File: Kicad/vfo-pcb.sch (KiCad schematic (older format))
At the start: 56 parts, among them J10 Link-out 1a, J11 RxTx, J13 Link-out 1b, J14 V12, J17 Link-out 2a, J18 Link-out 3, J19 Link-out 2b, J2 Conn_01x07_Female, J3 Si5351, J4 ESP32L, J5 ESP32R, J6 Rotery Encoder1, J7 ILI9341, J8 Rotery Encoder2, J9 Analog in 3-6, SW1 Rotary_Encoder_Switch, U1 AS179-92LF, U2 74HC595, U3 L7805, U4 AS179-92LF

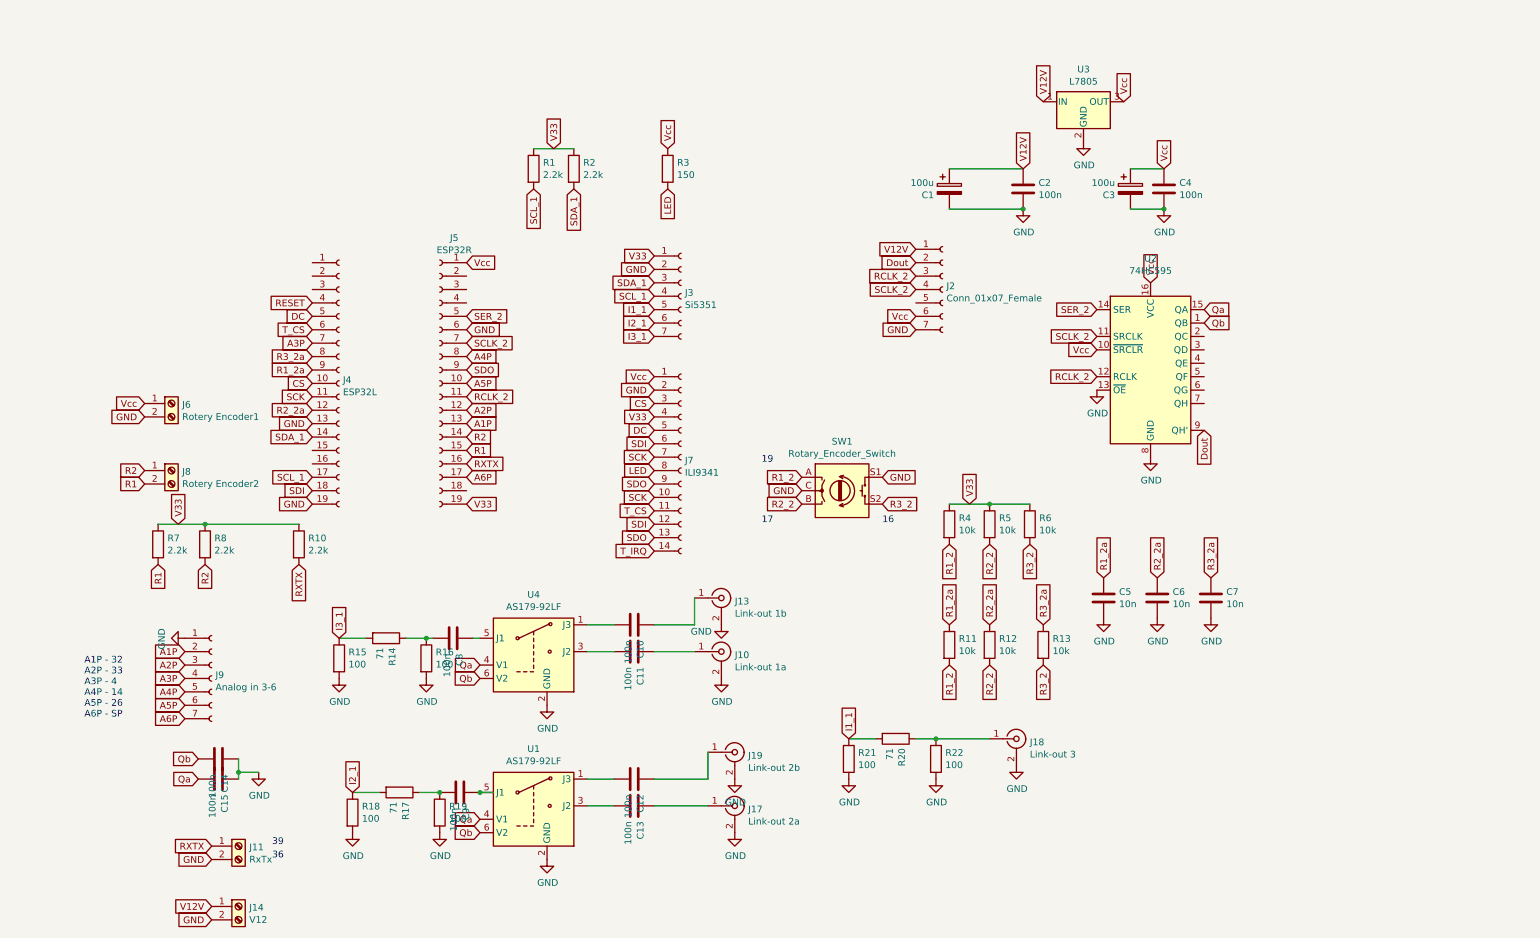
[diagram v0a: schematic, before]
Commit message: Attenuator removed
To improve crosstalk the attenuators are removed and replaced by 100nF DC blocker
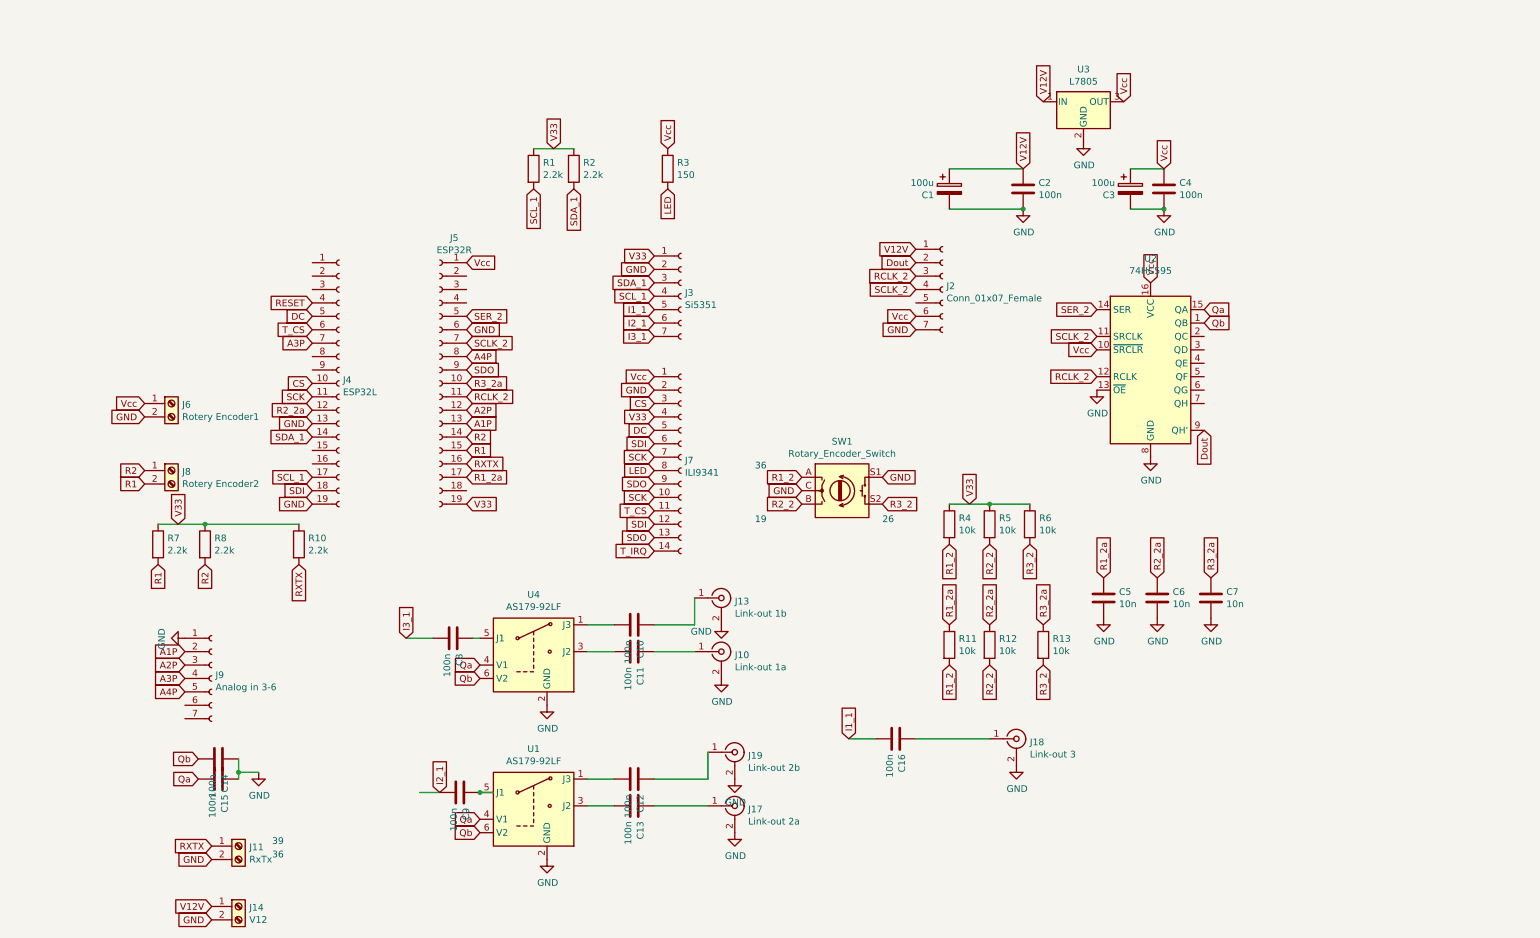
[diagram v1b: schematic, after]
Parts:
- removed R14, R17, R20: 71, Resistor_SMD:R_1206_3216Metric_Pad1.42x1.75mm_HandSolder, symbol Device:R
- removed R15, R16, R18, R19, R21, R22: 100, Resistor_SMD:R_1206_3216Metric_Pad1.42x1.75mm_HandSolder, symbol Device:R
- added C16: 100n, Capacitor_SMD:C_1206_3216Metric_Pad1.42x1.75mm_HandSolder, symbol Device:C
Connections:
- net labels removed: A5P, A6P
- wire segments 32 -> 28
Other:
- note added: "26"
- note removed: "16"
- note removed: "17"
- note removed: "A1P - 32\nA2P - 33\nA3P - 4\nA4P - 14\nA5P - 26\nA6P - SP"
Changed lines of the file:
@@
 Text GLabel 6400 4100 0    50   Input ~ 0
 R2_2
-Text GLabel 2750 3100 0    50   Input ~ 0
+Text GLabel 3900 3900 2    50   Input ~ 0
 R1_2a
-Text GLabel 2750 3400 0    50   Input ~ 0
-R2_2a
 Text GLabel 7000 4100 2    50   Input ~ 0
 R3_2
-Text GLabel 2750 3000 0    50   Input ~ 0
+Text GLabel 3900 3200 2    50   Input ~ 0
 R3_2a
 Text GLabel 7000 3900 2    50   Input ~ 0
@@
 Text GLabel 6750 5850 1    50   Input ~ 0
 I1_1
-Text GLabel 3050 6250 1    50   Input ~ 0
+Text GLabel 3700 6250 1    50   Input ~ 0
 I2_1
 $Comp
@@
 Text GLabel 8650 4650 1    50   Input ~ 0
 R1_2a
-$Comp
-L power:GND #PWR014
-U 1 1 5DAB08FF
-P 2950 5400
-F 0 "#PWR014" H 2950 5150 50  0001 C CNN
-F 1 "GND" H 2955 5227 50  0000 C CNN
-F 2 "" H 2950 5400 50  0001 C CNN
-F 3 "" H 2950 5400 50  0001 C CNN
-	1    2950 5400
-	1    0    0    -1
-$EndComp
-$Comp
-L Device:R R15
-U 1 1 5DABA121
-P 2950 5250
-F 0 "R15" H 3020 5296 50  0000 L CNN
-F 1 "100" H 3020 5205 50  0000 L CNN
-F 2 "Resistor_SMD:R_1206_3216Metric_Pad1.42x1.75mm_HandSolder" V 2880 5250 50  0001 C CNN
-F 3 "~" H 2950 5250 50  0001 C CNN
-	1    2950 5250
-	1    0    0    -1
-$EndComp
-$Comp
-L power:GND #PWR015
-U 1 1 5DABB0D6
-P 3600 5400
-F 0 "#PWR015" H 3600 5150 50  0001 C CNN
-F 1 "GND" H 3605 5227 50  0000 C CNN
-F 2 "" H 3600 5400 50  0001 C CNN
-F 3 "" H 3600 5400 50  0001 C CNN
-	1    3600 5400
-	1    0    0    -1
-$EndComp
-$Comp
-L Device:R R16
-U 1 1 5DABB0E0
-P 3600 5250
-F 0 "R16" H 3670 5296 50  0000 L CNN
-F 1 "100" H 3670 5205 50  0000 L CNN
-F 2 "Resistor_SMD:R_1206_3216Metric_Pad1.42x1.75mm_HandSolder" V 3530 5250 50  0001 C CNN
-F 3 "~" H 3600 5250 50  0001 C CNN
-	1    3600 5250
-	1    0    0    -1
-$EndComp
-$Comp
-L Device:R R14
-U 1 1 5DABC06A
-P 3300 5100
-F 0 "R14" H 3370 5146 50  0000 L CNN
-F 1 "71" H 3370 5055 50  0000 L CNN
-F 2 "Resistor_SMD:R_1206_3216Metric_Pad1.42x1.75mm_HandSolder" V 3230 5100 50  0001 C CNN
-F 3 "~" H 3300 5100 50  0001 C CNN
-	1    3300 5100
-	0    1    1    0
-$EndComp
-Wire Wire Line
-	3450 5100 3600 5100
-Wire Wire Line
-	2950 5100 3150 5100
-$Comp
-L power:GND #PWR016
-U 1 1 5DABF436
-P 3050 6550
-F 0 "#PWR016" H 3050 6300 50  0001 C CNN
-F 1 "GND" H 3055 6377 50  0000 C CNN
-F 2 "" H 3050 6550 50  0001 C CNN
-F 3 "" H 3050 6550 50  0001 C CNN
-	1    3050 6550
-	1    0    0    -1
-$EndComp
-$Comp
-L Device:R R18
-U 1 1 5DABF440
-P 3050 6400
-F 0 "R18" H 3120 6446 50  0000 L CNN
-F 1 "100" H 3120 6355 50  0000 L CNN
-F 2 "Resistor_SMD:R_1206_3216Metric_Pad1.42x1.75mm_HandSolder" V 2980 6400 50  0001 C CNN
-F 3 "~" H 3050 6400 50  0001 C CNN
-	1    3050 6400
-	1    0    0    -1
-$EndComp
-$Comp
-L power:GND #PWR017
-U 1 1 5DABF44A
-P 3700 6550
-F 0 "#PWR017" H 3700 6300 50  0001 C CNN
-F 1 "GND" H 3705 6377 50  0000 C CNN
-F 2 "" H 3700 6550 50  0001 C CNN
-F 3 "" H 3700 6550 50  0001 C CNN
-	1    3700 6550
-	1    0    0    -1
-$EndComp
-$Comp
-L Device:R R19
-U 1 1 5DABF454
-P 3700 6400
-F 0 "R19" H 3770 6446 50  0000 L CNN
-F 1 "100" H 3770 6355 50  0000 L CNN
-F 2 "Resistor_SMD:R_1206_3216Metric_Pad1.42x1.75mm_HandSolder" V 3630 6400 50  0001 C CNN
-F 3 "~" H 3700 6400 50  0001 C CNN
-	1    3700 6400
-	1    0    0    -1
-$EndComp
-$Comp
-L Device:R R17
-U 1 1 5DABF45E
-P 3400 6250
-F 0 "R17" H 3470 6296 50  0000 L CNN
-F 1 "71" H 3470 6205 50  0000 L CNN
-F 2 "Resistor_SMD:R_1206_3216Metric_Pad1.42x1.75mm_HandSolder" V 3330 6250 50  0001 C CNN
-F 3 "~" H 3400 6250 50  0001 C CNN
-	1    3400 6250
-	0    1    1    0
-$EndComp
 Wire Wire Line
 	3550 6250 3700 6250
-Wire Wire Line
-	3050 6250 3250 6250
 Text GLabel 2750 2900 0    50   Input ~ 0
 A3P
 Text GLabel 3900 3000 2    50   Input ~ 0
 A4P
-Text GLabel 3900 3900 2    50   Input ~ 0
-A6P
-Text GLabel 3900 3200 2    50   Input ~ 0
-A5P
 $Comp
 L Connector:Conn_01x07_Female J9
@@
 	1    0    0    -1
 $EndComp
-Text GLabel 1800 5600 0    50   Input ~ 0
-A5P
 Text GLabel 1800 5500 0    50   Input ~ 0
 A4P
@@
 	0    1    1    0
 $EndComp
-Text GLabel 2950 5100 1    50   Input ~ 0
+Text GLabel 3450 5100 1    50   Input ~ 0
 I3_1
-Wire Wire Line
-	7400 5850 7800 5850
-$Comp
-L power:GND #PWR021
-U 1 1 5DEE6825
-P 6750 6150
-F 0 "#PWR021" H 6750 5900 50  0001 C CNN
-F 1 "GND" H 6755 5977 50  0000 C CNN
-F 2 "" H 6750 6150 50  0001 C CNN
-F 3 "" H 6750 6150 50  0001 C CNN
-	1    6750 6150
-	1    0    0    -1
-$EndComp
-$Comp
-L Device:R R21
-U 1 1 5DEE682F
-P 6750 6000
-F 0 "R21" H 6820 6046 50  0000 L CNN
-F 1 "100" H 6820 5955 50  0000 L CNN
-F 2 "Resistor_SMD:R_1206_3216Metric_Pad1.42x1.75mm_HandSolder" V 6680 6000 50  0001 C CNN
-F 3 "~" H 6750 6000 50  0001 C CNN
-	1    6750 6000
-	1    0    0    -1
-$EndComp
-$Comp
-L power:GND #PWR022
-U 1 1 5DEE6839
-P 7400 6150
-F 0 "#PWR022" H 7400 5900 50  0001 C CNN
-F 1 "GND" H 7405 5977 50  0000 C CNN
-F 2 "" H 7400 6150 50  0001 C CNN
-F 3 "" H 7400 6150 50  0001 C CNN
-	1    7400 6150
-	1    0    0    -1
-$EndComp
-$Comp
-L Device:R R22
-U 1 1 5DEE6843
-P 7400 6000
-F 0 "R22" H 7470 6046 50  0000 L CNN
-F 1 "100" H 7470 5955 50  0000 L CNN
-F 2 "Resistor_SMD:R_1206_3216Metric_Pad1.42x1.75mm_HandSolder" V 7330 6000 50  0001 C CNN
-F 3 "~" H 7400 6000 50  0001 C CNN
-	1    7400 6000
-	1    0    0    -1
-$EndComp
-$Comp
-L Device:R R20
-U 1 1 5DEE684D
-P 7100 5850
-F 0 "R20" H 7170 5896 50  0000 L CNN
-F 1 "71" H 7170 5805 50  0000 L CNN
-F 2 "Resistor_SMD:R_1206_3216Metric_Pad1.42x1.75mm_HandSolder" V 7030 5850 50  0001 C CNN
-F 3 "~" H 7100 5850 50  0001 C CNN
-	1    7100 5850
-	0    1    1    0
-$EndComp
-Wire Wire Line
-	7250 5850 7400 5850
-Connection ~ 7400 5850
 Wire Wire Line
 	6750 5850 6950 5850
@@
 Text GLabel 3900 3600 2    50   Input ~ 0
 R2
-Text Notes 6100 3800 0    50   ~ 0
+Text Notes 6050 4250 0    50   ~ 0
 19
-Text Notes 6100 4250 0    50   ~ 0
-17
 Text Notes 7000 4250 0    50   ~ 0
-16
+26
 Text Notes 2450 6650 0    50   ~ 0
 39
@@
 Text GLabel 1800 5200 0    50   Input ~ 0
 A1P
-Text GLabel 1800 5700 0    50   Input ~ 0
-A6P
 $Comp
 L Device:C C8
@@
 $EndComp
 Wire Wire Line
-	3600 5100 3650 5100
-Connection ~ 3600 5100
-Wire Wire Line
 	3950 5100 4000 5100
 $Comp
@@
 	0    -1   -1   0
 $EndComp
-Connection ~ 3700 6250
 Connection ~ 4000 6250
 $Comp
@@
 Wire Wire Line
 	1950 4250 2650 4250
-Text Notes 1050 5700 0    50   ~ 0
-A1P - 32\nA2P - 33\nA3P - 4\nA4P - 14\nA5P - 26\nA6P - SP
+Text GLabel 2750 3400 0    50   Input ~ 0
+R2_2a
+Text Notes 6050 3850 0    50   ~ 0
+36
+$Comp
+L Device:C C16
+U 1 1 5EBF9AAC
+P 7100 5850
+F 0 "C16" H 6985 5804 50  0000 R CNN
+F 1 "100n" H 6985 5895 50  0000 R CNN
+F 2 "Capacitor_SMD:C_1206_3216Metric_Pad1.42x1.75mm_HandSolder" H 7138 5700 50  0001 C CNN
+F 3 "~" H 7100 5850 50  0001 C CNN
+	1    7100 5850
+	0    -1   -1   0
+$EndComp
+Wire Wire Line
+	7250 5850 7800 5850
+Wire Wire Line
+	3450 5100 3650 5100
 $EndSCHEMATC

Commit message: Add files via upload
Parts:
- removed J18: Link-out 3, Connector_Coaxial:SMA_Amphenol_132134_Vertical, symbol Connector:Conn_Coaxial
- removed J3: Si5351, Connector_PinSocket_2.54mm:PinSocket_1x07_P2.54mm_Vertical, symbol Connector:Conn_01x07_Female
- removed U1, U4: AS179-92LF, Package_TO_SOT_SMD:SOT-363_SC-70-6, symbol RF_Switch:AS179-92LF
- removed U2: 74HC595, Package_DIP:DIP-16_W7.62mm_LongPads, symbol 74xx:74HC595
- added C17, C18, C19, C20, C21, C22, C23: 100n, Capacitor_SMD:C_1206_3216Metric_Pad1.42x1.75mm_HandSolder, symbol Device:C
- added J12: Link-out 1-2, Connector_Coaxial:SMA_Amphenol_132134_Vertical, symbol Connector:Conn_Coaxial
- added J15: Link-out 2-2, Connector_Coaxial:SMA_Amphenol_132134_Vertical, symbol Connector:Conn_Coaxial
- added Q1, Q2, Q3, Q4, Q5, Q6: BFR92, Package_TO_SOT_SMD:SOT-323_SC-70, symbol Transistor_BJT135:BFR92
- added R13, R14: 2.2k, Resistor_SMD:R_1206_3216Metric_Pad1.42x1.75mm_HandSolder, symbol Device:R
- added R15, R16, R17, R21, R22, R23: 1k, Resistor_SMD:R_1206_3216Metric_Pad1.42x1.75mm_HandSolder, symbol Device:R
- added R18, R19, R20, R24, R25, R26: 47, Resistor_SMD:R_1206_3216Metric_Pad1.42x1.75mm_HandSolder, symbol Device:R
- added U2, U3: Si5351A-B-GT, Package_SO:MSOP-10_3x3mm_P0.5mm, symbol Oscillator:Si5351A-B-GT
- added U4: AMS1117, Package_TO_SOT_SMD:SOT-223-3_TabPin2, symbol Regulator_Linear:AMS1117
- added Y1, Y2: Crystal, Crystal:Crystal_SMD_TXC_7M-4Pin_3.2x2.5mm_HandSoldering, symbol Device:Crystal
- C16: value 100n -> 10u
- J10: renamed from J13; value Link-out 1b -> Link-out 1-0
- J11: renamed from J10; value Link-out 1a -> Link-out 1-1
- J13: renamed from J19; value Link-out 2b -> Link-out 2-0
- J14: renamed from J17; value Link-out 2a -> Link-out 2-1
- renumbered C5 to C3, C3 to C4, C6 to C5, C4 to C6, J6 to J1, J8 to J2, J9 to J3, J11 to J4, J14 to J5, J4 to J6, J5 to J7, J7 to J8, J2 to J9, R7 to R1, R12 to R10, R6 to R11, R13 to R12, R8 to R2, R10 to R3, R1 to R4, R2 to R5, R3 to R6, R4 to R7, R11 to R8, R5 to R9, U3 to U1
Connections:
- net labels added: SCL_2, SDA_2, V33a
- net labels removed: Dout, I1_1, I2_1, I3_1, Qa, Qb
- wire segments 28 -> 58
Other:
- moved on the sheet: C1, C2, C3, C4, C5, C6, C7, J1, J10, J11, J13, J14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

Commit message: Add files via upload
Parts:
- removed C10, C11, C12, C13, C14, C15: 100n, Capacitor_SMD:C_1206_3216Metric_Pad1.42x1.75mm_HandSolder, symbol Device:C
- Q1, Q2, Q3, Q4, Q5, Q6: footprint Package_TO_SOT_SMD:SOT-323_SC-70 -> Package_TO_SOT_SMD:SOT-23
- R18, R19, R20, R24, R25: value 47 -> 20
- Y1, Y2: symbol Device:Crystal -> Device:Crystal_GND2_Small
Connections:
- net GND: now also Y1.2, Y2.2; no longer R18.1, R19.1, R20.1, R24.1, R25.1, R26.1
- net at J13.1 (In): now also R18.2
- net at J14.1 (In): now also R20.2
- net at J10.1 (In): now also R24.2
- net at J11.1 (In): now also R26.2
- net at U2.2 (XA): now also Y1.1; no longer Y1.2
- net at U2.3 (XB): now also Y1.3; no longer Y1.1
- net at U3.2 (XA): now also Y2.1; no longer Y2.2
- net at U3.3 (XB): now also Y2.3; no longer Y2.1
- net at J12.1 (In): now also R25.2
- net at J15.1 (In): now also R19.2
- net at Q1.2 (E): now also R18.1; no longer R18.2
- net at Q2.2 (E): now also R19.1; no longer R19.2
- net at Q3.2 (E): now also R20.1; no longer R20.2
- net at Q4.2 (E): now also R24.1; no longer R24.2
- net at Q6.2 (E): now also R26.1; no longer R26.2
- net at Q5.2 (E): now also R25.1; no longer R25.2
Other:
- moved on the sheet: R18, R19, R20, R24, R25, R26

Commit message: Add files via upload
Updated output circuit added pi attenuation
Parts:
- added R21, R22, R23, R24, R25, R29, R32, R33, R34, R36, R37, R38: 150, Resistor_SMD:R_1206_3216Metric_Pad1.42x1.75mm_HandSolder, symbol Device:R
- R26: renamed from R18; value 20 -> 33
- R27: renamed from R19; value 20 -> 33
- R28: renamed from R24; value 20 -> 33
- R30: renamed from R25; value 20 -> 33
- R31: renamed from R20; value 20 -> 33
- R35: renamed from R26; value 47 -> 33
- renumbered C16 to C1, C4 to C10, C5 to C11, C6 to C12, C7 to C13, C9 to C14, C8 to C15, C18 to C16, C19 to C17, C17 to C2, C20 to C3, C21 to C4, C22 to C5, C1 to C6, C23 to C7, C2 to C8, C3 to C9, J12 to J10, J10 to J11, J13 to J12, J15 to J13, J11 to J15, Q4 to Q3, Q5 to Q4, Q3 to Q5, R12 to R10, R4 to R11, R13 to R12, R5 to R13, R21 to R18, R22 to R19, R23 to R20, R6 to R4, R7 to R5, R8 to R6, R9 to R7, R10 to R8, R11 to R9, U4 to U1, U1 to U2, U2 to U4, Y2 to Y1, Y1 to Y2
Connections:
- net GND: now also R21.2, R22.2, R23.2, R24.2, R25.2, R29.2, R32.2, R33.2, R34.2, R36.2, R37.2, R38.2
- net at J12.1 (In), R26.2: now also R33.1
- net at J14.1 (In), R31.2: now also R37.1
- net at J11.1 (In), R28.2: now also R32.1
- net at J15.1 (In), R35.2: now also R38.1
- net at J10.1 (In), R30.2: now also R36.1
- net at J13.1 (In), R27.2: now also R34.1
- net at Q1.2 (E), R26.1: now also R21.1
- net at Q5.2 (E), R31.1: now also R25.1
- net at Q2.2 (E), R27.1: now also R22.1
- net at Q3.2 (E), R28.1: now also R23.1
- net at Q6.2 (E), R35.1: now also R29.1
- net at Q4.2 (E), R30.1: now also R24.1
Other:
- moved on the sheet: J10, J11, J12, J13, J15, R26, R27, R28, R30, R35
